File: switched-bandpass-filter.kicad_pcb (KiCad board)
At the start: 2 copper layers, 82.1 x 72.6 mm, 69 parts, among them J1 SMA, J10 F3 out, J11 F4 out, J2 SMA, J3 F4 in, J4 , J5 F3 in, J6 F2 in, J7 F1 in, J8 F1 out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

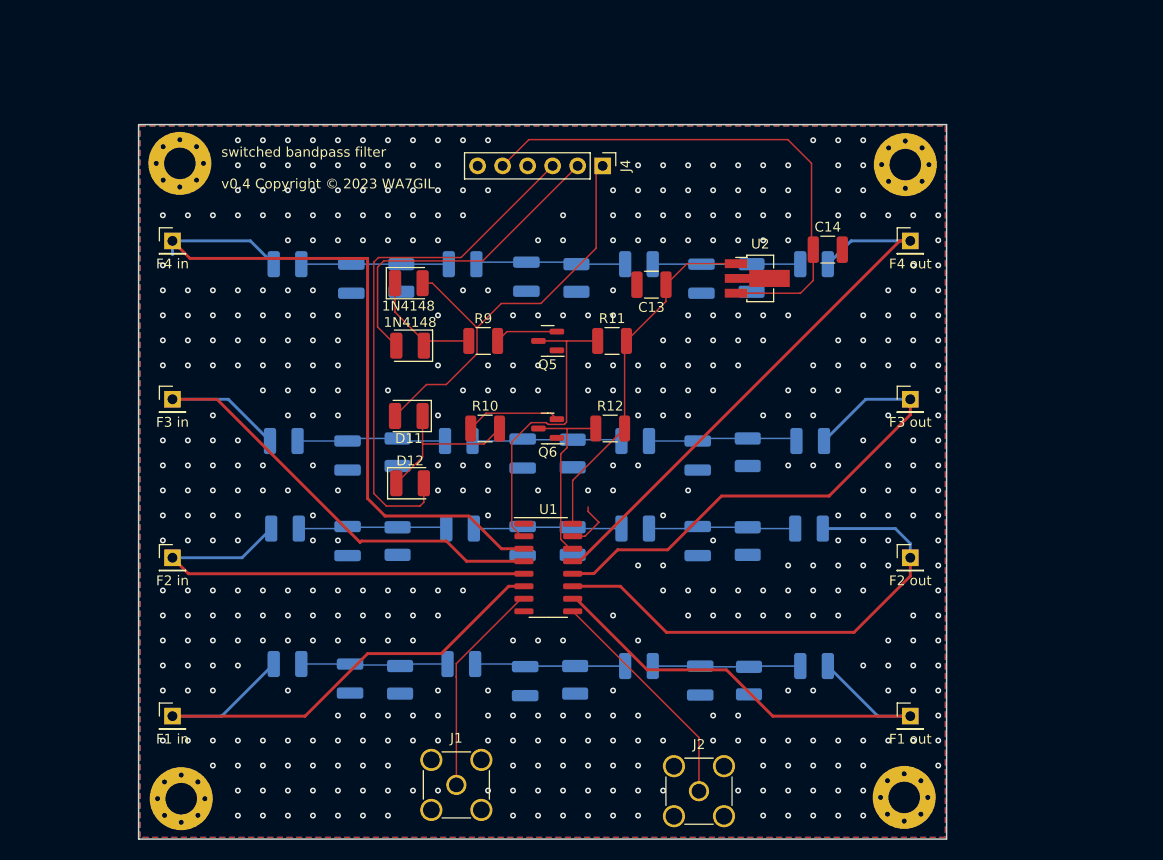
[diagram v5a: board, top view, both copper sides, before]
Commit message: v0.5 SMA traces now 0.3mm for 50 ohms
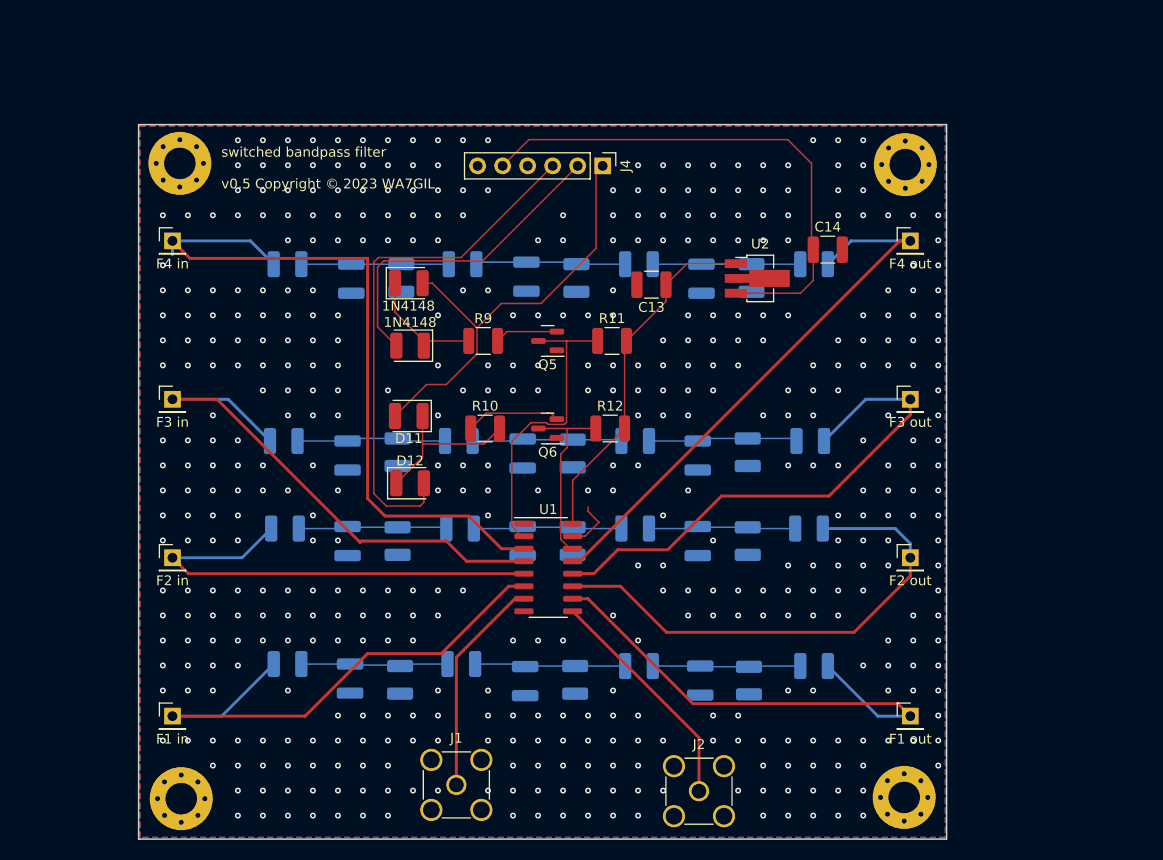
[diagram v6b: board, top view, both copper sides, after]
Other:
- board text added: "switched bandpass filter v0.5 Copyright © 2023 WA7GIL"
- board text removed: "switched bandpass filter v0.4 Copyright © 2023 WA7GIL"
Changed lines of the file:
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@@
   (paper "USLetter")
   (title_block
-    (comment 1 "board size 115x75mm")
+    (date "2023-07-23")
+    (rev "v0.5")
+    (comment 1 "board size 83x73mm")
     (comment 2 "Copyright © 2023 Ron Taylor WA7GIL")
   )
@@
     (effects (font (size 1 1) (thickness 0.15)) (justify left bottom mirror))
   )
-  (gr_text "switched bandpass filter\n\nv0.4 Copyright © 2023 WA7GIL  " (at 96.393 67.183) (layer "F.SilkS")
+  (gr_text "switched bandpass filter\n\nv0.5 Copyright © 2023 WA7GIL  " (at 96.393 67.183) (layer "F.SilkS")
     (effects (font (size 1 1) (thickness 0.15)) (justify left bottom))
   )
@@
   (segment (start 116.97 98.93) (end 116.97 97) (width 0.1524) (layer "F.Cu") (net 9))
   (segment (start 120.7394 74.0786) (end 112.3574 74.0786) (width 0.1524) (layer "F.Cu") (net 9))
-  (segment (start 127.13 108.73) (end 126.8494 108.73) (width 0.1524) (layer "F.Cu") (net 10))
-  (segment (start 120.2597 115.3197) (end 120.2597 116.667) (width 0.1524) (layer "F.Cu") (net 10))
-  (segment (start 126.8494 108.73) (end 120.2597 115.3197) (width 0.1524) (layer "F.Cu") (net 10))
-  (segment (start 120.269 116.6763) (end 120.269 127.635) (width 0.1524) (layer "F.Cu") (net 10))
-  (segment (start 120.2597 116.667) (end 120.269 116.6763) (width 0.1524) (layer "F.Cu") (net 10))
-  (segment (start 144.907 122.827) (end 144.907 128.27) (width 0.1524) (layer "F.Cu") (net 11))
-  (segment (start 132.08 110) (end 144.907 122.827) (width 0.1524) (layer "F.Cu") (net 11))
+  (segment (start 120.269 114.681) (end 126.22 108.73) (width 0.3) (layer "F.Cu") (net 10))
+  (segment (start 126.22 108.73) (end 127.13 108.73) (width 0.3) (layer "F.Cu") (net 10))
+  (segment (start 120.269 127.635) (end 120.269 114.681) (width 0.3) (layer "F.Cu") (net 10))
+  (segment (start 144.907 122.827) (end 144.907 128.27) (width 0.3) (layer "F.Cu") (net 11))
+  (segment (start 132.08 110) (end 144.907 122.827) (width 0.3) (layer "F.Cu") (net 11))
   (segment (start 121.539 100.33) (end 113.03 100.33) (width 0.3) (layer "F.Cu") (net 12))
   (segment (start 127.13 103.65) (end 124.859 103.65) (width 0.3) (layer "F.Cu") (net 12))
@@
   (segment (start 96.433 120.65) (end 91.44 120.65) (width 0.3) (layer "B.Cu") (net 17))
   (segment (start 101.724 115.359) (end 96.433 120.65) (width 0.3) (layer "B.Cu") (net 17))
-  (segment (start 139.64579 115.951) (end 147.701 115.951) (width 0.3) (layer "F.Cu") (net 18))
-  (segment (start 147.701 115.951) (end 152.4 120.65) (width 0.3) (layer "F.Cu") (net 18))
-  (segment (start 132.42479 108.73) (end 139.64579 115.951) (width 0.3) (layer "F.Cu") (net 18))
-  (segment (start 132.08 108.73) (end 132.42479 108.73) (width 0.3) (layer "F.Cu") (net 18))
-  (segment (start 152.4 120.65) (end 166.37 120.65) (width 0.3) (layer "F.Cu") (net 18))
-  (segment (start 157.994 115.564) (end 163.08 120.65) (width 0.3) (layer "B.Cu") (net 18))
-  (segment (start 163.08 120.65) (end 166.37 120.65) (width 0.3) (layer "B.Cu") (net 18))
+  (segment (start 165.1 119.38) (end 144.284577 119.38) (width 0.3) (layer "F.Cu") (net 18))
+  (segment (start 133.634577 108.73) (end 132.08 108.73) (width 0.3) (layer "F.Cu") (net 18))
+  (segment (start 144.284577 119.38) (end 133.634577 108.73) (width 0.3) (layer "F.Cu") (net 18))
+  (segment (start 166.37 120.65) (end 165.1 119.38) (width 0.3) (layer "F.Cu") (net 18))
+  (segment (start 166.37 120.65) (end 163.08 120.65) (width 0.3) (layer "B.Cu") (net 18))
+  (segment (start 163.08 120.65) (end 157.994 115.564) (width 0.3) (layer "B.Cu") (net 18))
   (segment (start 166.37 106.426) (end 166.37 104.5633) (width 0.3) (layer "F.Cu") (net 19))
   (segment (start 132.08 107.46) (end 136.924 107.46) (width 0.3) (layer "F.Cu") (net 19))

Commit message: removed stitched ground plane and shifted filter #3 to make space for 3mm gap in silk screen
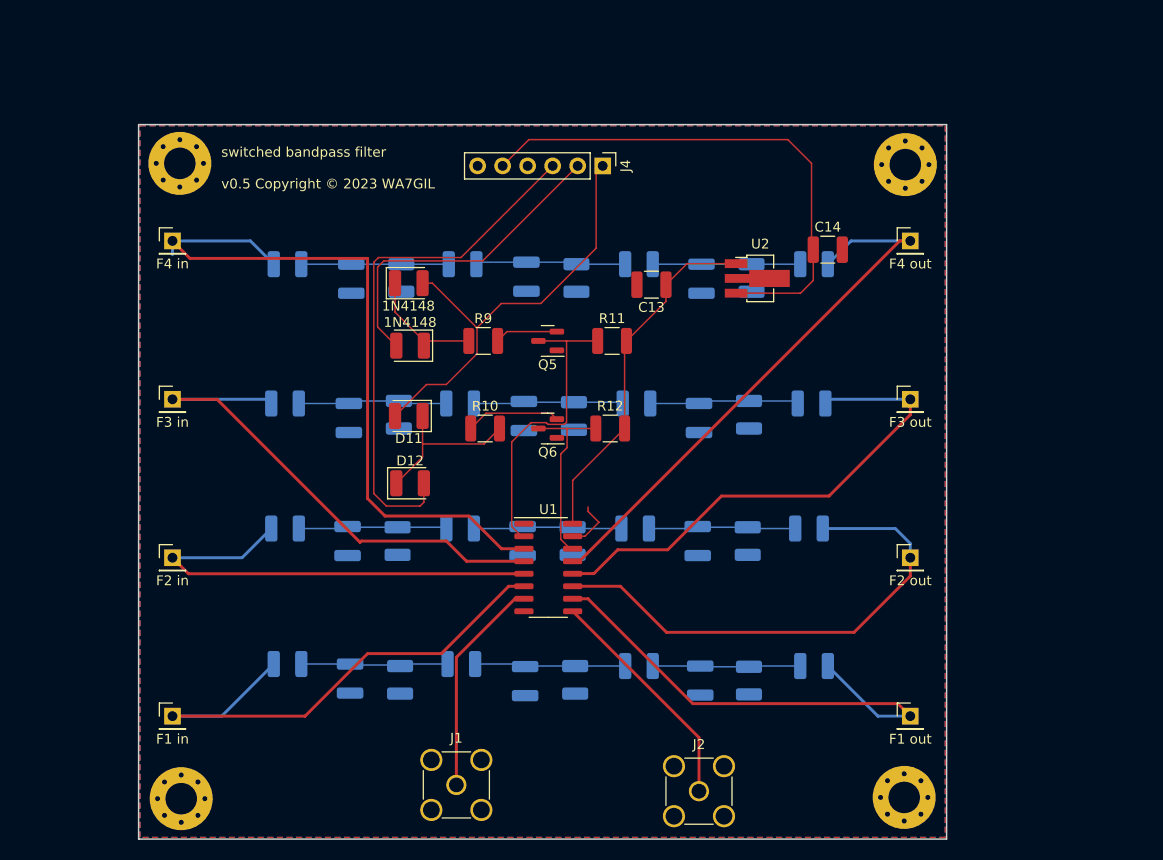
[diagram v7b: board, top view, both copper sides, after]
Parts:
- moved C11 3.81 mm to (109.3, 90.4)
- moved C7 3.81 mm to (144.9, 90.4)
- moved C9 3.81 mm to (127.1, 90.2)
- moved L21 3.81 mm to (132.2, 90.2)
- moved L15 3.81 mm to (156.3, 88.9)
- moved L17 3.81 mm to (150.0, 90.0)
- moved L19 3.81 mm to (138.6, 88.9)
- moved L23 3.81 mm to (120.6, 88.9)
- moved L25 3.81 mm to (114.4, 90.0)
- moved L27 3.81 mm to (102.9, 88.9)
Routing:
- net F3 out: track 53.1 -> 51.4 mm
- net F3 in: track 54.3 -> 52.8 mm
- net GND: vias 474 -> 0

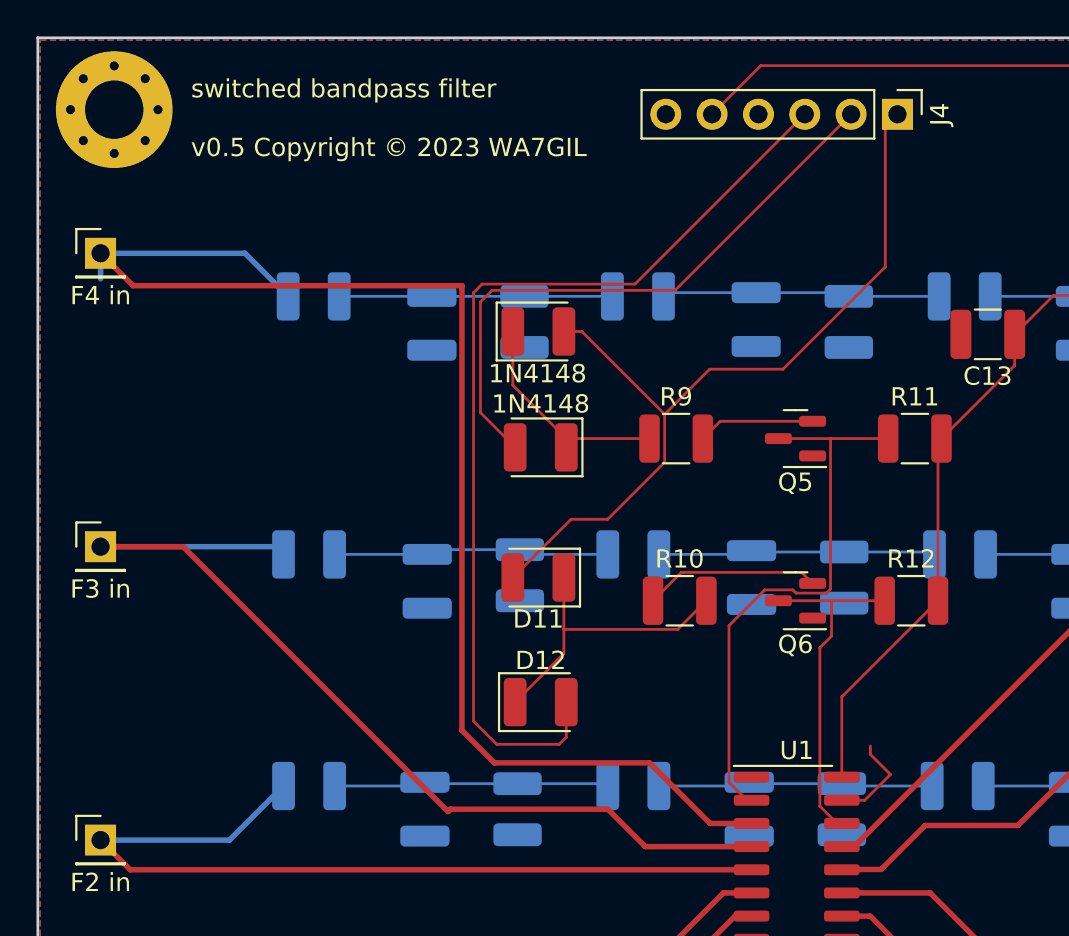
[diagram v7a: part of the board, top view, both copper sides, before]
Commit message: slowly approaching cutting out 3mm strips from solder mask on rear
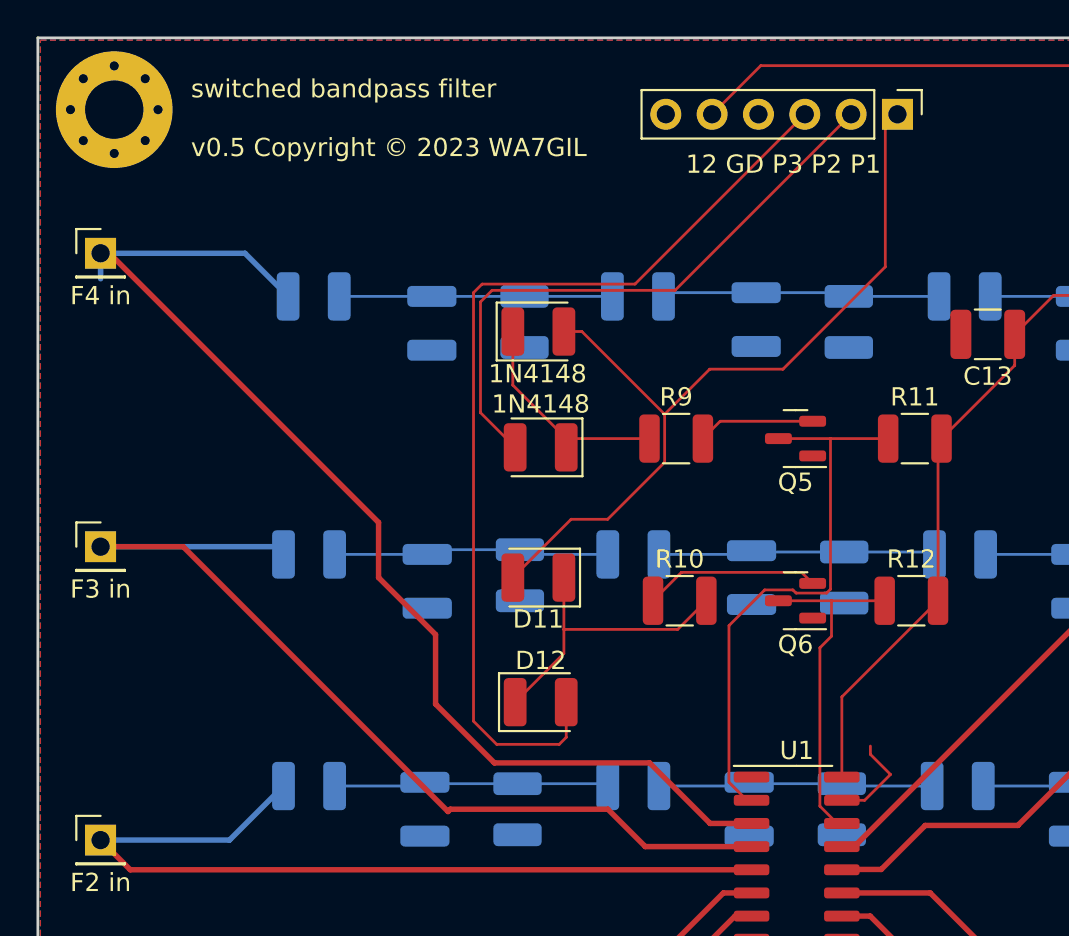
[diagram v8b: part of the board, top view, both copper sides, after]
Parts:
- renumbered J4 to 1
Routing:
- net F4 in: track 75.6 -> 65.3 mm
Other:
- board text added: "12 GD P3 P2 P1"
